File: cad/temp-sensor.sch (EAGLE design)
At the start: 60 parts, among them Q1 300S14-U, Q2 320S14-U, Q3 320S14-U, U1 SE555D, U2 SE555D, U4 MCP6001UT-I/OT, U5 MCP6001UT-I/OT, U6 MCP6001UT-I/OT, U7 MCP6001UT-I/OT, U8 NCV4264-2CST50T3G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

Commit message: Initialize layout file
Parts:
- added J2: (no value), SparkFun-Connectors:CONN_02
- added R21, R24: 10k, SparkFun-Resistors:10KOHM-0603-1/10W-1%
- added S1: MOMENTARY-SWITCH-SPST-PTH-6.0MM, SparkFun-Switches:MOMENTARY-SWITCH-SPST-PTH-6.0MM
- R18: value 10k -> 43k; device SparkFun-Resistors:10KOHM-0603-1/10W-1% -> SparkFun-Resistors:43KOHM-0603-1/10W-1%
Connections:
- new net PBTN: R24.1, S1.2, U9.PC1(ADC1)
- new net PULSE_TRIG: R21.1, U1.TRIG, U9.PD7(AIN1)
- new net START_C: Q3.B4, Q3.C2, R18.1
- net +5V: now also Q3.E2, Q3.E4, R21.2, R24.2; no longer R18.2
- net 555_RST_N: no longer R18.1
- net GND: now also R18.2, S1.1
- net PTAT_BASE: now also Q3.B2
- net SCL: now also J2.2
- net SDA: now also J2.1
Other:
- moved on the sheet: C10, C2, C4, R10, R12, R14, R15, R17, R18, R9

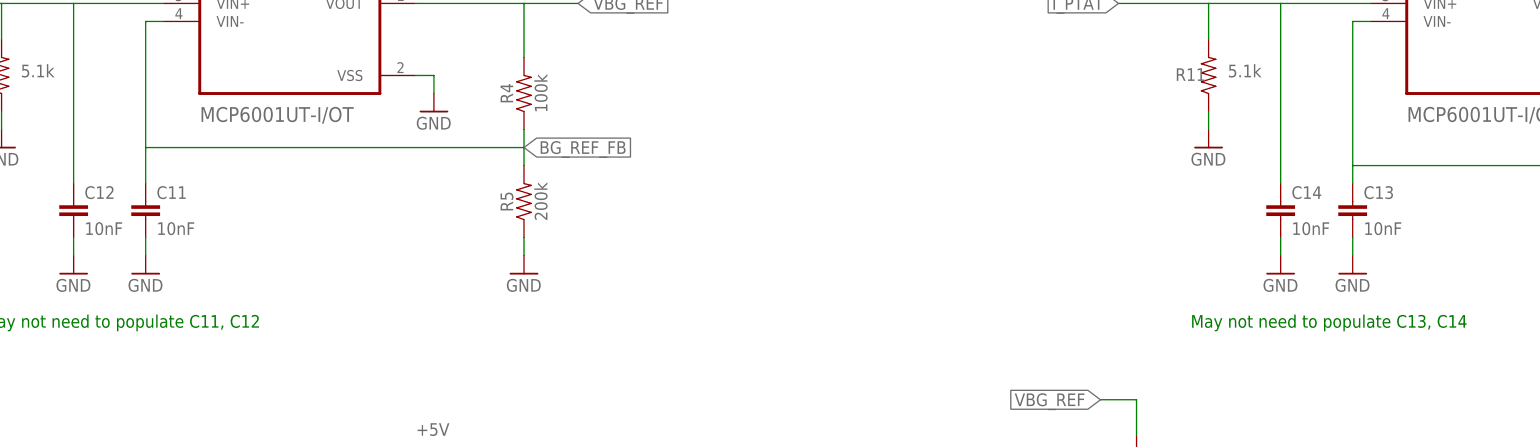
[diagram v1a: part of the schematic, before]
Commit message: Finalized Schematic and Layout
Got rid of C11 and C13 since they were causing oscillations
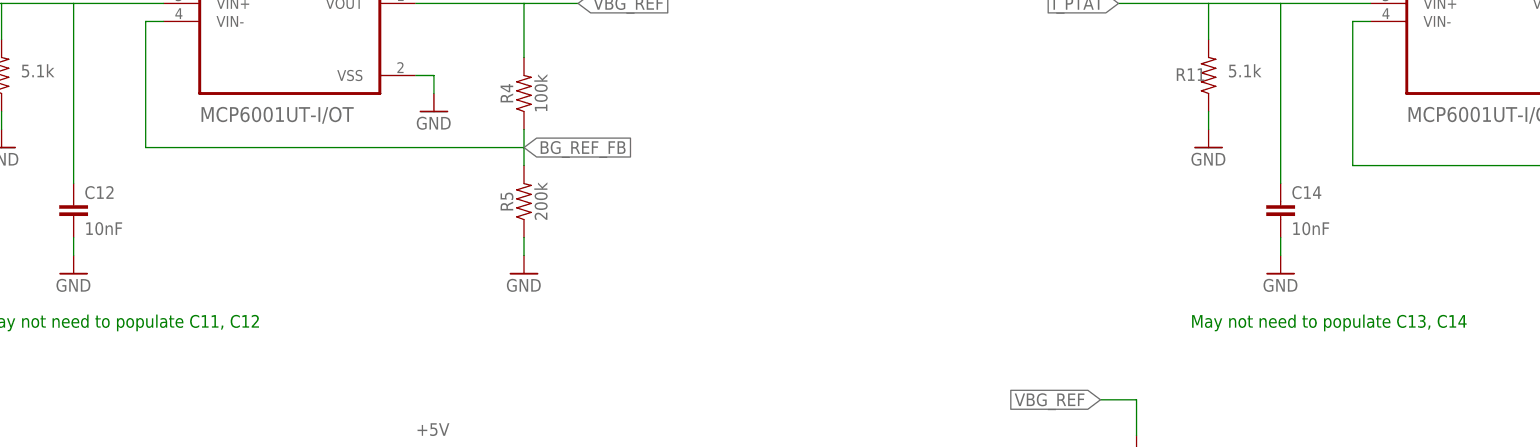
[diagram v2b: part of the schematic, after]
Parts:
- removed C11, C13: 10nF, SparkFun-Capacitors:10NF-0603-50V-10%
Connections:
- net BG_REF_FB: no longer C11.1
- net GND: no longer C11.2, C13.2
- net PTAT_REF_FB: no longer C13.1
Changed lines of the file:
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@@
 <part name="R13" library="SparkFun-Resistors" library_urn="urn:adsk.eagle:library:532" deviceset="0OHM" device="-0603-1/10W" package3d_urn="urn:adsk.eagle:package:41389018/1" value="0"/>
 <part name="GND23" library="supply1" library_urn="urn:adsk.eagle:library:371" deviceset="GND" device=""/>
-<part name="C11" library="SparkFun-Capacitors" library_urn="urn:adsk.eagle:library:510" deviceset="10NF" device="-0603-50V-10%" package3d_urn="urn:adsk.eagle:package:41385090/1" value="10nF"/>
-<part name="GND27" library="supply1" library_urn="urn:adsk.eagle:library:371" deviceset="GND" device=""/>
 <part name="C12" library="SparkFun-Capacitors" library_urn="urn:adsk.eagle:library:510" deviceset="10NF" device="-0603-50V-10%" package3d_urn="urn:adsk.eagle:package:41385090/1" value="10nF"/>
 <part name="GND28" library="supply1" library_urn="urn:adsk.eagle:library:371" deviceset="GND" device=""/>
-<part name="C13" library="SparkFun-Capacitors" library_urn="urn:adsk.eagle:library:510" deviceset="10NF" device="-0603-50V-10%" package3d_urn="urn:adsk.eagle:package:41385090/1" value="10nF"/>
-<part name="GND29" library="supply1" library_urn="urn:adsk.eagle:library:371" deviceset="GND" device=""/>
 <part name="C14" library="SparkFun-Capacitors" library_urn="urn:adsk.eagle:library:510" deviceset="10NF" device="-0603-50V-10%" package3d_urn="urn:adsk.eagle:package:41385090/1" value="10nF"/>
 <part name="GND30" library="supply1" library_urn="urn:adsk.eagle:library:371" deviceset="GND" device=""/>
@@
 <attribute name="VALUE" x="248.92" y="71.12" size="1.778" layer="96"/>
 </instance>
-<instance part="C11" gate="G$1" x="27.94" y="83.82" smashed="yes">
-<attribute name="NAME" x="29.464" y="86.741" size="1.778" layer="95" font="vector"/>
-<attribute name="VALUE" x="29.464" y="81.661" size="1.778" layer="96" font="vector"/>
-</instance>
-<instance part="GND27" gate="1" x="27.94" y="76.2" smashed="yes">
-<attribute name="VALUE" x="25.4" y="73.66" size="1.778" layer="96"/>
-</instance>
 <instance part="C12" gate="G$1" x="17.78" y="83.82" smashed="yes">
 <attribute name="NAME" x="19.304" y="86.741" size="1.778" layer="95" font="vector"/>
@@
 <instance part="GND28" gate="1" x="17.78" y="76.2" smashed="yes">
 <attribute name="VALUE" x="15.24" y="73.66" size="1.778" layer="96"/>
-</instance>
-<instance part="C13" gate="G$1" x="198.12" y="83.82" smashed="yes">
-<attribute name="NAME" x="199.644" y="86.741" size="1.778" layer="95" font="vector"/>
-<attribute name="VALUE" x="199.644" y="81.661" size="1.778" layer="96" font="vector"/>
-</instance>
-<instance part="GND29" gate="1" x="198.12" y="76.2" smashed="yes">
-<attribute name="VALUE" x="195.58" y="73.66" size="1.778" layer="96"/>
 </instance>
 <instance part="C14" gate="G$1" x="187.96" y="83.82" smashed="yes">
@@
 </segment>
 <segment>
-<wire x1="27.94" y1="81.28" x2="27.94" y2="78.74" width="0.1524" layer="91"/>
-<pinref part="GND27" gate="1" pin="GND"/>
-<pinref part="C11" gate="G$1" pin="2"/>
-</segment>
-<segment>
 <wire x1="17.78" y1="81.28" x2="17.78" y2="78.74" width="0.1524" layer="91"/>
 <pinref part="GND28" gate="1" pin="GND"/>
 <pinref part="C12" gate="G$1" pin="2"/>
-</segment>
-<segment>
-<wire x1="198.12" y1="81.28" x2="198.12" y2="78.74" width="0.1524" layer="91"/>
-<pinref part="GND29" gate="1" pin="GND"/>
-<pinref part="C13" gate="G$1" pin="2"/>
 </segment>
 <segment>
@@
 <pinref part="R5" gate="G$1" pin="2"/>
 <label x="81.28" y="93.98" size="1.778" layer="95" xref="yes"/>
-<pinref part="C11" gate="G$1" pin="1"/>
-<wire x1="27.94" y1="88.9" x2="27.94" y2="93.98" width="0.1524" layer="91"/>
 </segment>
 </net>
@@
 <wire x1="198.12" y1="111.76" x2="200.66" y2="111.76" width="0.1524" layer="91"/>
 <label x="251.46" y="91.44" size="1.778" layer="95" xref="yes"/>
-<pinref part="C13" gate="G$1" pin="1"/>
-<wire x1="198.12" y1="88.9" x2="198.12" y2="91.44" width="0.1524" layer="91"/>
-</segment>
-</net>
+</segment>
+</net>

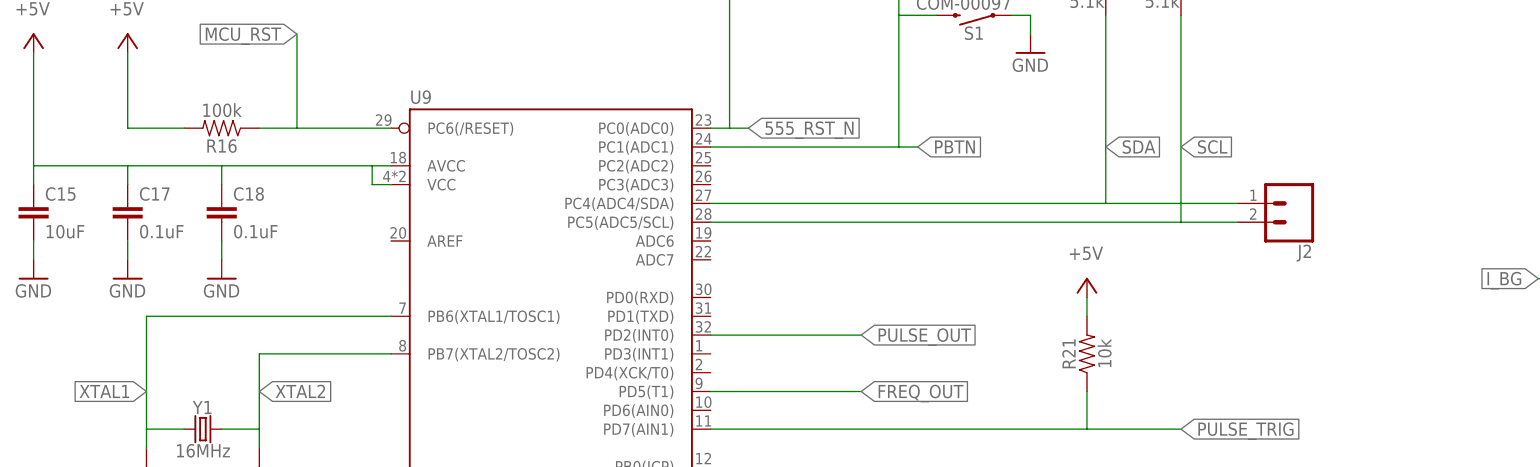
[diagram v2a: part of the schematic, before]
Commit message: Edit placement
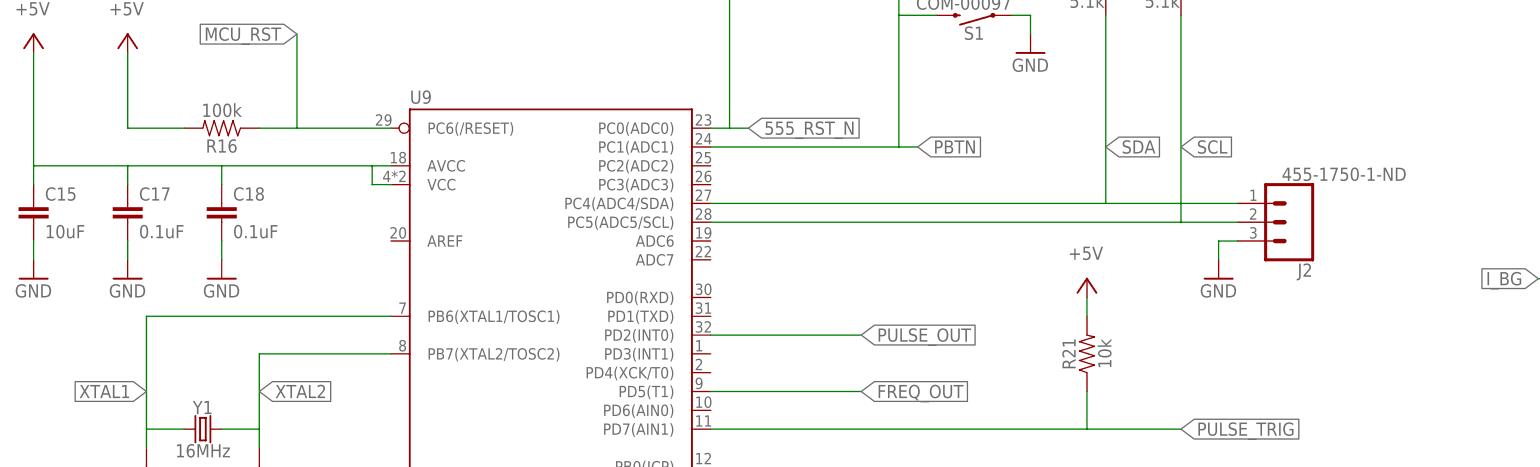
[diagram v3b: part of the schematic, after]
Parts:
- J2: value (none) -> 455-1750-1-ND; device SparkFun-Connectors:CONN_02 -> SparkFun-Connectors:CONN_03
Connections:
- removed net N$1: C17.1
- net +5V: now also C17.1
- net GND: now also J2.3
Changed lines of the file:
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@@
 <part name="P+20" library="supply1" library_urn="urn:adsk.eagle:library:371" deviceset="+5V" device=""/>
 <part name="GND46" library="supply1" library_urn="urn:adsk.eagle:library:371" deviceset="GND" device=""/>
-<part name="J2" library="SparkFun-Connectors" library_urn="urn:adsk.eagle:library:513" deviceset="CONN_02" device="" package3d_urn="urn:adsk.eagle:package:38039/2"/>
 <part name="S1" library="SparkFun-Switches" library_urn="urn:adsk.eagle:library:535" deviceset="MOMENTARY-SWITCH-SPST" device="-PTH-6.0MM" package3d_urn="urn:adsk.eagle:package:40163/2"/>
 <part name="GND47" library="supply1" library_urn="urn:adsk.eagle:library:371" deviceset="GND" device=""/>
@@
 <part name="P+12" library="supply1" library_urn="urn:adsk.eagle:library:371" deviceset="+5V" device=""/>
 <part name="R21" library="SparkFun-Resistors" library_urn="urn:adsk.eagle:library:532" deviceset="10KOHM" device="-0603-1/10W-1%" package3d_urn="urn:adsk.eagle:package:41389018/1" value="10k"/>
+<part name="J2" library="SparkFun-Connectors" library_urn="urn:adsk.eagle:library:513" deviceset="CONN_03" device="" package3d_urn="urn:adsk.eagle:package:38063/2" value="455-1750-1-ND"/>
+<part name="GND27" library="supply1" library_urn="urn:adsk.eagle:library:371" deviceset="GND" device=""/>
 </parts>
 <sheets>
@@
 <attribute name="VALUE" x="99.06" y="198.12" size="1.778" layer="96"/>
 </instance>
-<instance part="J2" gate="J1" x="-38.1" y="124.46" smashed="yes" rot="R180">
-<attribute name="VALUE" x="-35.56" y="129.286" size="1.778" layer="96" font="vector" rot="R180"/>
-<attribute name="NAME" x="-35.56" y="118.872" size="1.778" layer="95" font="vector" rot="R180"/>
-</instance>
 <instance part="S1" gate="G$1" x="-81.28" y="149.86" smashed="yes" rot="R180">
 <attribute name="NAME" x="-81.28" y="148.336" size="1.778" layer="95" font="vector" rot="R180" align="bottom-center"/>
@@
 <attribute name="NAME" x="-67.564" y="104.14" size="1.778" layer="95" font="vector" rot="R90" align="bottom-center"/>
 <attribute name="VALUE" x="-64.516" y="104.14" size="1.778" layer="96" font="vector" rot="R90" align="top-center"/>
+</instance>
+<instance part="J2" gate="J1" x="-38.1" y="121.92" smashed="yes" rot="R180">
+<attribute name="VALUE" x="-22.86" y="129.286" size="1.778" layer="96" font="vector" rot="R180"/>
+<attribute name="NAME" x="-35.56" y="116.332" size="1.778" layer="95" font="vector" rot="R180"/>
+</instance>
+<instance part="GND27" gate="1" x="-48.26" y="114.3" smashed="yes">
+<attribute name="VALUE" x="-50.8" y="111.76" size="1.778" layer="96"/>
 </instance>
 </instances>
@@
 <wire x1="-73.66" y1="149.86" x2="-73.66" y2="147.32" width="0.1524" layer="91"/>
 <pinref part="GND47" gate="1" pin="GND"/>
+</segment>
+<segment>
+<wire x1="-48.26" y1="119.38" x2="-48.26" y2="116.84" width="0.1524" layer="91"/>
+<pinref part="GND27" gate="1" pin="GND"/>
+<pinref part="J2" gate="J1" pin="3"/>
+<wire x1="-48.26" y1="119.38" x2="-45.72" y2="119.38" width="0.1524" layer="91"/>
 </segment>
 </net>
@@
 <pinref part="C18" gate="G$1" pin="1"/>
 <wire x1="-182.88" y1="127" x2="-182.88" y2="129.54" width="0.1524" layer="91"/>
-<wire x1="-182.88" y1="129.54" x2="-208.28" y2="129.54" width="0.1524" layer="91"/>
+<wire x1="-182.88" y1="129.54" x2="-195.58" y2="129.54" width="0.1524" layer="91"/>
 <pinref part="U9" gate="U1" pin="AVCC"/>
 <pinref part="U9" gate="U1" pin="VCC"/>
+<wire x1="-195.58" y1="129.54" x2="-208.28" y2="129.54" width="0.1524" layer="91"/>
 <wire x1="-162.56" y1="127" x2="-160.02" y2="127" width="0.1524" layer="91"/>
 <wire x1="-162.56" y1="127" x2="-162.56" y2="129.54" width="0.1524" layer="91"/>
 <wire x1="-162.56" y1="129.54" x2="-160.02" y2="129.54" width="0.1524" layer="91"/>
 <wire x1="-182.88" y1="129.54" x2="-162.56" y2="129.54" width="0.1524" layer="91"/>
+<pinref part="C17" gate="G$1" pin="1"/>
+<wire x1="-195.58" y1="127" x2="-195.58" y2="129.54" width="0.1524" layer="91"/>
 </segment>
 <segment>
@@
 </segment>
 </net>
-<net name="N$1" class="0">
-<segment>
-<pinref part="C17" gate="G$1" pin="1"/>
-<wire x1="-195.58" y1="127" x2="-195.58" y2="129.54" width="0.1524" layer="91"/>
-</segment>
-</net>

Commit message: Edit placement again
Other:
- note removed: "May not need to populate C11, C12"
- note removed: "May not need to populate C13, C14"
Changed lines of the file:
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@@
 <text x="203.2" y="40.64" size="1.778" layer="91">U2 is in astable mode</text>
 <text x="259.08" y="83.82" size="1.778" layer="91">DO NOT POPULATE R6</text>
-<text x="175.26" y="68.58" size="1.778" layer="91">May not need to populate C13, C14</text>
-<text x="5.08" y="68.58" size="1.778" layer="91">May not need to populate C11, C12</text>
 <text x="-129.54" y="238.76" size="1.778" layer="91">LDO Voltage Regulator</text>
 <text x="-165.1" y="226.06" size="1.778" layer="91">Battery connection</text>
